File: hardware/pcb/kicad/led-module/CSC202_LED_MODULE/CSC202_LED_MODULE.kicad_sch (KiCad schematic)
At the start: 25 parts, among them J1 SPI_TAP, J2 PWR_ENTRY, J3 LED_IF, J4 SPI_IF, J6 EN_IF, SW1 SPI↔BUF, U1 CA56-12SEKWA, U2 74HC244, U3 74HC595

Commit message: added reverse polarity protection and included bottom assy in outputs
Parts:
- added D2: D_Schottky, symbol Device:D_Schottky
- renumbered J6 to J5
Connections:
- net at JP1.1 (A): now also D2.1 (K); no longer J2.1 (Pin_1)
- new net: D2.2 (A), J2.1 (Pin_1)
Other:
- moved on the sheet: J5, JP1
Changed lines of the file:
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@@
 		(rev "A")
 		(company "Eli Bell")
+		(comment 1 "allowing the module to demonstrate both parallel GPIO control and serial output expansion.")
+		(comment 2 "or through an SPI shift register interface. A jumper shunt selects the control mode, ")
+		(comment 3 "The LEDs and display segments can be driven either directly via GPIO (current sinking) ")
+		(comment 4 "A visual output board featuring an 8-LED bar graph and a 4-digit seven-segment display. ")
 	)
 	(rectangle
@@
 	)
 	(junction
-		(at 40.64 152.4)
-		(diameter 0)
-		(color 0 0 0 0)
-	)
-	(junction
 		(at 67.31 64.77)
 		(diameter 0)
@@
 	)
 	(junction
-		(at 40.64 149.86)
-		(diameter 0)
-		(color 0 0 0 0)
-	)
-	(junction
 		(at 143.51 48.26)
 		(diameter 0)
@@
 	)
 	(junction
-		(at 40.64 154.94)
-		(diameter 0)
-		(color 0 0 0 0)
-	)
-	(junction
 		(at 217.17 134.62)
 		(diameter 0)
@@
 	)
 	(junction
-		(at 40.64 157.48)
-		(diameter 0)
-		(color 0 0 0 0)
-	)
-	(junction
 		(at 130.81 139.7)
 		(diameter 0)
@@
 		(color 0 0 0 0)
 	)
-	(junction
-		(at 40.64 147.32)
-		(diameter 0)
-		(color 0 0 0 0)
-	)
 	(no_connect
 		(at 214.63 149.86)
@@
 	(wire
 		(pts
-			(xy 39.37 152.4) (xy 40.64 152.4)
-		)
-		(stroke
-			(width 0)
-			(type default)
-		)
-	)
-	(wire
-		(pts
 			(xy 137.16 35.56) (xy 128.27 35.56)
 		)
@@
 	(wire
 		(pts
-			(xy 39.37 149.86) (xy 40.64 149.86)
+			(xy 39.37 149.86) (xy 49.53 149.86)
 		)
 		(stroke
@@
 	(wire
 		(pts
-			(xy 40.64 149.86) (xy 49.53 149.86)
-		)
-		(stroke
-			(width 0)
-			(type default)
-		)
-	)
-	(wire
-		(pts
 			(xy 40.64 101.6) (xy 50.8 101.6)
 		)
@@
 	(wire
 		(pts
-			(xy 40.64 154.94) (xy 49.53 154.94)
+			(xy 39.37 154.94) (xy 49.53 154.94)
 		)
 		(stroke
@@
 		)
 	)
-	(wire
-		(pts
-			(xy 39.37 157.48) (xy 40.64 157.48)
-		)
-		(stroke
-			(width 0)
-			(type default)
-		)
-	)
 	(bus
 		(pts
@@
 	(wire
 		(pts
-			(xy 55.88 68.58) (xy 63.5 68.58)
+			(xy 62.23 68.58) (xy 63.5 68.58)
 		)
 		(stroke
@@
 	(wire
 		(pts
-			(xy 40.64 68.58) (xy 45.72 68.58)
+			(xy 40.64 68.58) (xy 43.18 68.58)
 		)
 		(stroke
@@
 	(wire
 		(pts
-			(xy 40.64 157.48) (xy 49.53 157.48)
+			(xy 39.37 157.48) (xy 49.53 157.48)
 		)
 		(stroke
@@
 	(wire
 		(pts
-			(xy 40.64 147.32) (xy 49.53 147.32)
+			(xy 39.37 147.32) (xy 49.53 147.32)
 		)
 		(stroke
@@
 	(wire
 		(pts
-			(xy 40.64 152.4) (xy 49.53 152.4)
+			(xy 39.37 152.4) (xy 49.53 152.4)
 		)
 		(stroke
@@
 	(wire
 		(pts
+			(xy 50.8 68.58) (xy 52.07 68.58)
+		)
+		(stroke
+			(width 0)
+			(type default)
+		)
+	)
+	(wire
+		(pts
 			(xy 118.11 109.22) (xy 107.95 109.22)
 		)
@@
 		)
 	)
-	(wire
-		(pts
-			(xy 39.37 154.94) (xy 40.64 154.94)
-		)
-		(stroke
-			(width 0)
-			(type default)
-		)
-	)
 	(bus
 		(pts
@@
 		)
 	)
-	(wire
-		(pts
-			(xy 39.37 147.32) (xy 40.64 147.32)
-		)
-		(stroke
-			(width 0)
-			(type default)
-		)
-	)
 	(label "MOSI"
 		(at 196.85 44.45 180)
@@
 	(symbol
 		(lib_id "Connector:Conn_01x05_Pin")
-		(at 35.56 152.4 0)
+		(at 34.29 152.4 0)
 		(unit 1)
 		(exclude_from_sim no)
@@
 		(on_board yes)
 		(dnp no)
-		(property "Reference" "J6"
-			(at 35.56 141.732 0)
+		(property "Reference" "J5"
+			(at 36.068 141.478 0)
 			(effects
 				(font
@@
 		)
 		(property "Value" "EN_IF"
-			(at 35.56 144.272 0)
+			(at 36.068 144.018 0)
 			(effects
 				(font
@@
 		)
 		(property "Footprint" "Connector_PinHeader_2.54mm:PinHeader_1x05_P2.54mm_Vertical"
-			(at 35.56 152.4 0)
+			(at 34.29 152.4 0)
 			(effects
 				(font
@@
 		)
 		(property "Datasheet" "~"
-			(at 35.56 152.4 0)
+			(at 34.29 152.4 0)
 			(effects
 				(font
@@
 		)
 		(property "Description" "Generic connector, single row, 01x05, script generated"
-			(at 35.56 152.4 0)
+			(at 34.29 152.4 0)
 			(effects
 				(font
@@
 			(project ""
 				(path "/501232f2-70a5-4b6c-b37f-05d55718ad93"
-					(reference "J6")
+					(reference "J5")
 					(unit 1)
 				)
@@
 	(symbol
 		(lib_id "Jumper:Jumper_2_Bridged")
-		(at 50.8 68.58 0)
+		(at 57.15 68.58 0)
 		(unit 1)
 		(exclude_from_sim yes)
@@
 		(dnp no)
 		(property "Reference" "JP1"
-			(at 50.8 63.5 0)
+			(at 57.15 63.5 0)
 			(effects
 				(font
@@
 		)
 		(property "Value" "TEST_PT"
-			(at 51.562 65.786 0)
+			(at 57.912 65.786 0)
 			(effects
 				(font
@@
 		)
 		(property "Footprint" "Connector_PinHeader_2.54mm:PinHeader_1x02_P2.54mm_Vertical"
-			(at 50.8 68.58 0)
+			(at 57.15 68.58 0)
 			(effects
 				(font
@@
 		)
 		(property "Datasheet" "~"
-			(at 50.8 68.58 0)
+			(at 57.15 68.58 0)
 			(effects
 				(font
@@
 		)
 		(property "Description" "Jumper, 2-pole, closed/bridged"
-			(at 50.8 68.58 0)
+			(at 57.15 68.58 0)
 			(effects
 				(font
@@
 					(unit 1)
 				)
+			)
+		)
+	)
+	(symbol
+		(lib_id "Device:D_Schottky")
+		(at 46.99 68.58 180)
+		(unit 1)
+		(exclude_from_sim no)
+		(in_bom yes)
+		(on_board yes)
+		(dnp no)
+		(fields_autoplaced yes)
+		(property "Reference" "D2"
+			(at 47.3075 62.23 0)
+			(effects
+				(font
+					(size 1.27 1.27)
+				)
+			)
+		)
+		(property "Value" "D_Schottky"
+			(at 47.3075 64.77 0)
+			(effects
+				(font
+					(size 1.27 1.27)
+				)
+			)
+		)
+		(property "Footprint" ""
+			(at 46.99 68.58 0)
+			(effects
+				(font
+					(size 1.27 1.27)
+				)
+				(hide yes)
+			)
+		)
+		(property "Datasheet" "~"
+			(at 46.99 68.58 0)
+			(effects
+				(font
+					(size 1.27 1.27)
+				)
+				(hide yes)
+			)
+		)
+		(property "Description" "Schottky diode"
+			(at 46.99 68.58 0)
+			(effects
+				(font
+					(size 1.27 1.27)
+				)
+				(hide yes)
+			)
+		)
+		(pin "1"
+		)
+		(pin "2"
+		)
+		(instances
+			(project ""
+				(path "/501232f2-70a5-4b6c-b37f-05d55718ad93"
+					(reference "D2")
+					(unit 1)
+				)

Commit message: update LED module KiCad design
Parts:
- D2: value D_Schottky -> 1N5817; footprint (none) -> Diode_THT:D_A-405_P12.70mm_Horizontal
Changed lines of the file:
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@@
 			)
 		)
-		(property "Value" "D_Schottky"
+		(property "Value" "1N5817"
 			(at 47.3075 64.77 0)
 			(effects
@@
 			)
 		)
-		(property "Footprint" ""
+		(property "Footprint" "Diode_THT:D_A-405_P12.70mm_Horizontal"
 			(at 46.99 68.58 0)
 			(effects

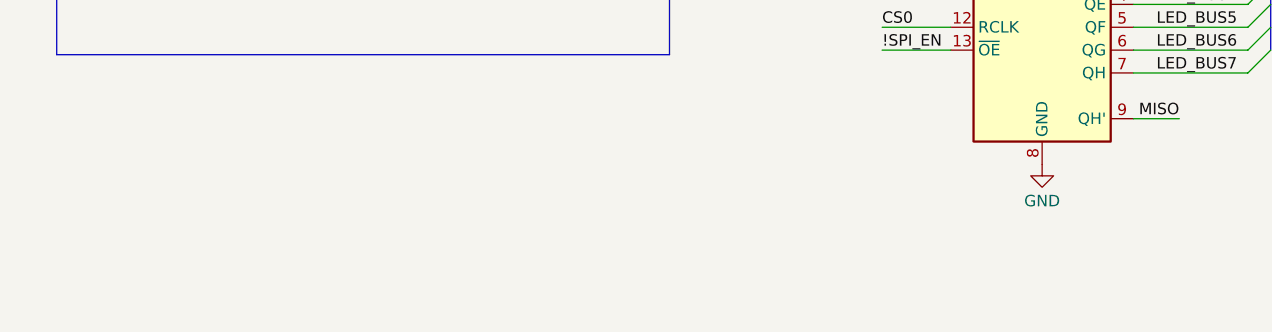
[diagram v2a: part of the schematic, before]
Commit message: note added to sch concerning backpowering
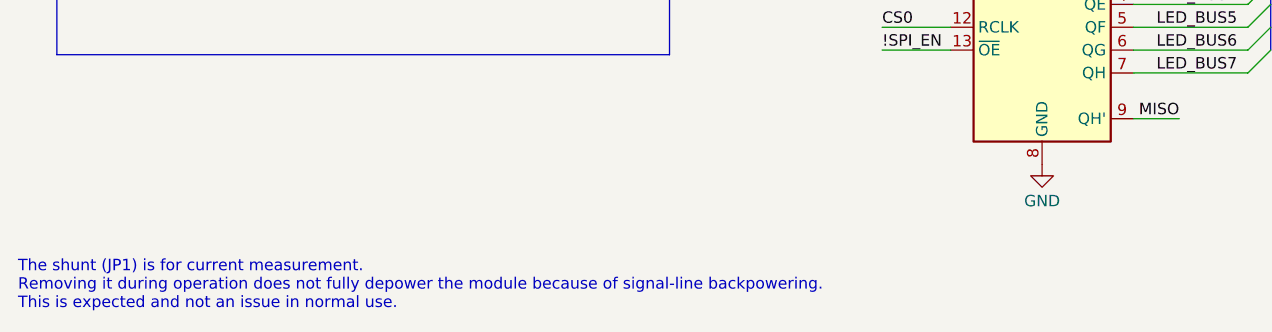
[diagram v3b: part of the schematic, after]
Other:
- note added: "The shunt (JP1) is for current measurement. Removing it during operation does not fully depower the module because of signal-line backpowering. This is expected and not an issue in normal use."
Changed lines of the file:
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@@
+		)
+	)
+	(text "The shunt (JP1) is for current measurement.\nRemoving it during operation does not fully depower the module because of signal-line backpowering.\nThis is expected and not an issue in normal use."
+		(exclude_from_sim no)
+		(at 17.018 191.262 0)
+		(effects
+			(font
+				(size 1.27 1.27)
+			)
+			(justify left)
 		)
 	)
